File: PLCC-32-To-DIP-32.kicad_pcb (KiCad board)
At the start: 2 copper layers, 41.9 x 19 mm, 2 parts, among them U1 27C080, U2 27C080

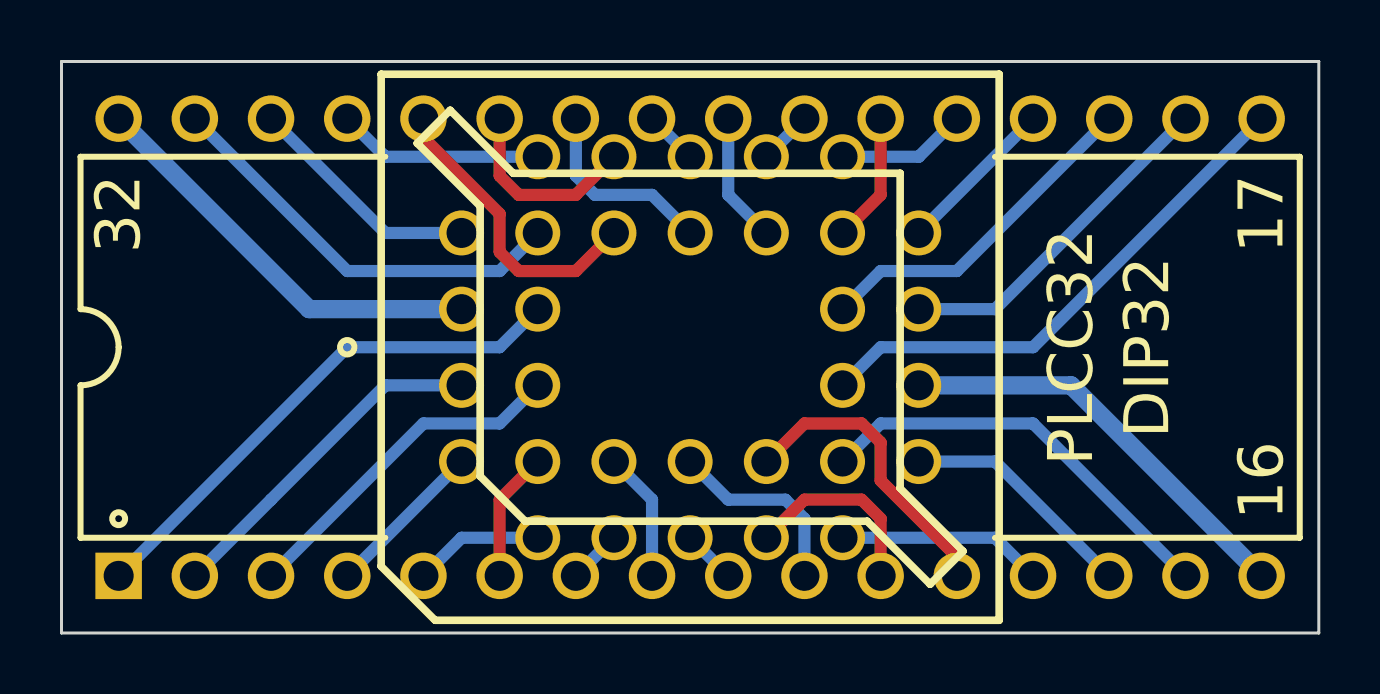
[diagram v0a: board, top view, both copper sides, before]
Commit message: Fixed gerber settings. Gerber output
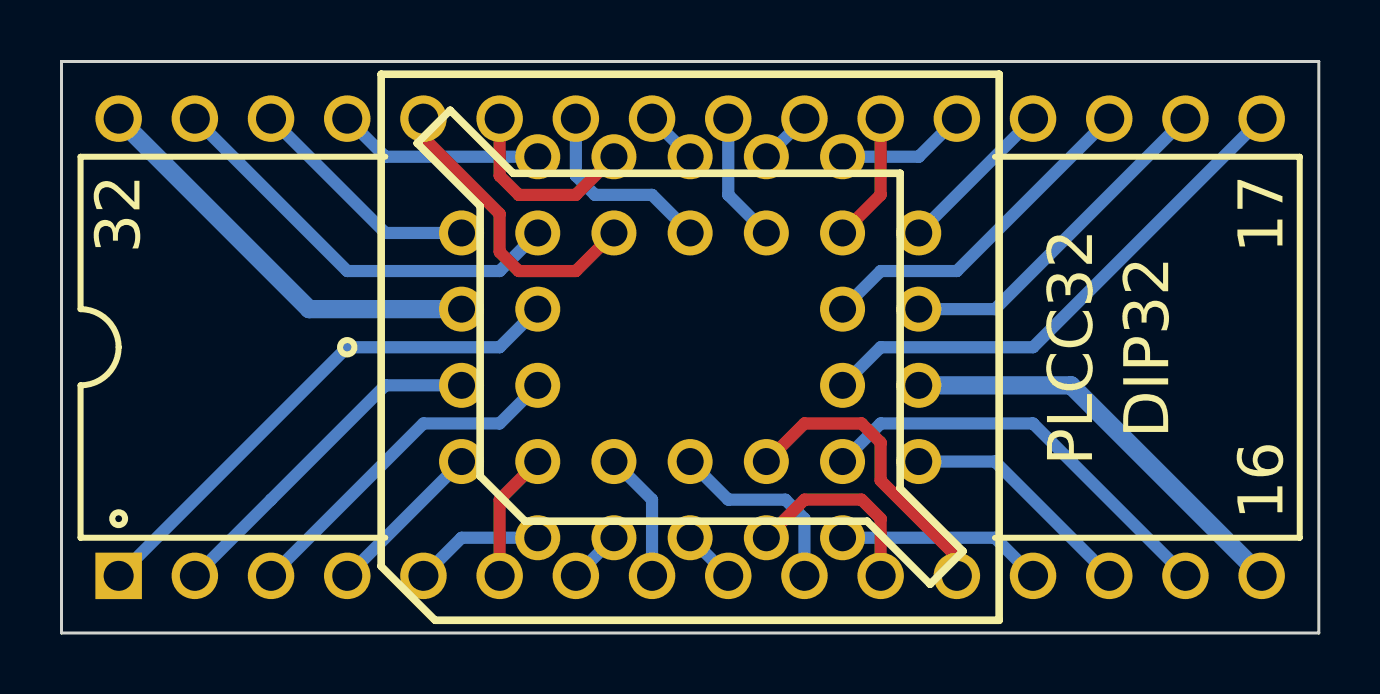
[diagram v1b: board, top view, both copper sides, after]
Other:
- rule pad_to_mask_clearance: 0 -> 0.1016
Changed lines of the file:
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@@
     (links 32)
     (no_connects 0)
-    (area 126.555499 95.834999 181.355 122.080001)
+    (area 127.584999 95.834999 181.355 122.080001)
     (thickness 1.6)
     (drawings 12)
@@
     (mod_text_width 0.1524)
     (pad_size 1.5 1.5)
-    (pad_drill 1)
-    (pad_to_mask_clearance 0)
-    (aux_axis_origin 0 0)
+    (pad_drill 0.9)
+    (pad_to_mask_clearance 0.1016)
+    (aux_axis_origin 127.635 114.935)
     (visible_elements FFFFFF7F)
     (pcbplotparams
-      (layerselection 3178497)
+      (layerselection 283148289)
       (usegerberextensions true)
       (excludeedgelayer true)
@@
       (viasonmask false)
       (mode 1)
-      (useauxorigin false)
+      (useauxorigin true)
       (hpglpennumber 1)
       (hpglpenspeed 20)
@@
       (plotinvisibletext false)
       (padsonsilk false)
-      (subtractmaskfromsilk false)
+      (subtractmaskfromsilk true)
       (outputformat 1)
       (mirror false)
-      (drillshape 1)
+      (drillshape 0)
       (scaleselection 1)
-      (outputdirectory ""))
+      (outputdirectory gerbers/))
   )
   (net 0 "")
@@
     (fp_line (start -7.8994 8.001) (end -6.79958 9.10082) (layer F.SilkS) (width 0.254))
     (fp_line (start -6.79958 9.09574) (end -4.70154 6.9977) (layer F.SilkS) (width 0.254))
-    (pad 2 thru_hole circle (at 1.27 7.62 270) (size 1.5 1.5) (drill 1)
+    (pad 2 thru_hole circle (at 1.27 7.62 270) (size 1.5 1.5) (drill 0.9)
       (layers *.Cu *.Mask F.SilkS)
       (net 9 /A16)
     )
-    (pad 1 thru_hole circle (at -1.27 5.08 270) (size 1.5 1.5) (drill 1)
+    (pad 1 thru_hole circle (at -1.27 5.08 270) (size 1.5 1.5) (drill 0.9)
       (layers *.Cu *.Mask F.SilkS)
       (net 12 /A19)
     )
-    (pad 3 thru_hole circle (at 1.27 5.08 270) (size 1.5 1.5) (drill 1)
+    (pad 3 thru_hole circle (at 1.27 5.08 270) (size 1.5 1.5) (drill 0.9)
       (layers *.Cu *.Mask F.SilkS)
       (net 8 /A15)
     )
-    (pad 4 thru_hole circle (at 3.81 7.62 270) (size 1.5 1.5) (drill 1)
+    (pad 4 thru_hole circle (at 3.81 7.62 270) (size 1.5 1.5) (drill 0.9)
       (layers *.Cu *.Mask F.SilkS)
       (net 5 /A12)
     )
-    (pad 5 thru_hole circle (at 6.35 5.08 270) (size 1.5 1.5) (drill 1)
+    (pad 5 thru_hole circle (at 6.35 5.08 270) (size 1.5 1.5) (drill 0.9)
       (layers *.Cu *.Mask F.SilkS)
       (net 18 /A7)
     )
-    (pad 6 thru_hole circle (at 3.81 5.08 270) (size 1.5 1.5) (drill 1)
+    (pad 6 thru_hole circle (at 3.81 5.08 270) (size 1.5 1.5) (drill 0.9)
       (layers *.Cu *.Mask F.SilkS)
       (net 17 /A6)
     )
-    (pad 7 thru_hole circle (at 6.35 2.54 270) (size 1.5 1.5) (drill 1)
+    (pad 7 thru_hole circle (at 6.35 2.54 270) (size 1.5 1.5) (drill 0.9)
       (layers *.Cu *.Mask F.SilkS)
       (net 16 /A5)
     )
-    (pad 8 thru_hole circle (at 3.81 2.54 270) (size 1.5 1.5) (drill 1)
+    (pad 8 thru_hole circle (at 3.81 2.54 270) (size 1.5 1.5) (drill 0.9)
       (layers *.Cu *.Mask F.SilkS)
       (net 15 /A4)
     )
-    (pad 9 thru_hole circle (at 6.35 0 270) (size 1.5 1.5) (drill 1)
+    (pad 9 thru_hole circle (at 6.35 0 270) (size 1.5 1.5) (drill 0.9)
       (layers *.Cu *.Mask F.SilkS)
       (net 14 /A3)
     )
-    (pad 10 thru_hole circle (at 3.81 0 270) (size 1.5 1.5) (drill 1)
+    (pad 10 thru_hole circle (at 3.81 0 270) (size 1.5 1.5) (drill 0.9)
       (layers *.Cu *.Mask F.SilkS)
       (net 13 /A2)
     )
-    (pad 11 thru_hole circle (at 6.35 -2.54 270) (size 1.5 1.5) (drill 1)
+    (pad 11 thru_hole circle (at 6.35 -2.54 270) (size 1.5 1.5) (drill 0.9)
       (layers *.Cu *.Mask F.SilkS)
       (net 2 /A1)
     )
-    (pad 12 thru_hole circle (at 3.81 -2.54 270) (size 1.5 1.5) (drill 1)
+    (pad 12 thru_hole circle (at 3.81 -2.54 270) (size 1.5 1.5) (drill 0.9)
       (layers *.Cu *.Mask F.SilkS)
       (net 1 /A0)
     )
-    (pad 13 thru_hole circle (at 6.35 -5.08 270) (size 1.5 1.5) (drill 1)
+    (pad 13 thru_hole circle (at 6.35 -5.08 270) (size 1.5 1.5) (drill 0.9)
       (layers *.Cu *.Mask F.SilkS)
       (net 22 /D0)
     )
-    (pad 14 thru_hole circle (at 3.81 -7.62 270) (size 1.5 1.5) (drill 1)
+    (pad 14 thru_hole circle (at 3.81 -7.62 270) (size 1.5 1.5) (drill 0.9)
       (layers *.Cu *.Mask F.SilkS)
       (net 23 /D1)
     )
-    (pad 15 thru_hole circle (at 3.81 -5.08 270) (size 1.5 1.5) (drill 1)
+    (pad 15 thru_hole circle (at 3.81 -5.08 270) (size 1.5 1.5) (drill 0.9)
       (layers *.Cu *.Mask F.SilkS)
       (net 24 /D2)
     )
-    (pad 16 thru_hole circle (at 1.27 -7.62 270) (size 1.5 1.5) (drill 1)
+    (pad 16 thru_hole circle (at 1.27 -7.62 270) (size 1.5 1.5) (drill 0.9)
       (layers *.Cu *.Mask F.SilkS)
       (net 31 GND)
     )
-    (pad 17 thru_hole circle (at 1.27 -5.08 270) (size 1.5 1.5) (drill 1)
+    (pad 17 thru_hole circle (at 1.27 -5.08 270) (size 1.5 1.5) (drill 0.9)
       (layers *.Cu *.Mask F.SilkS)
       (net 25 /D3)
     )
-    (pad 18 thru_hole circle (at -1.27 -7.62 270) (size 1.5 1.5) (drill 1)
+    (pad 18 thru_hole circle (at -1.27 -7.62 270) (size 1.5 1.5) (drill 0.9)
       (layers *.Cu *.Mask F.SilkS)
       (net 26 /D4)
     )
-    (pad 19 thru_hole circle (at -1.27 -5.08 270) (size 1.5 1.5) (drill 1)
+    (pad 19 thru_hole circle (at -1.27 -5.08 270) (size 1.5 1.5) (drill 0.9)
       (layers *.Cu *.Mask F.SilkS)
       (net 27 /D5)
     )
-    (pad 20 thru_hole circle (at -3.81 -7.62 270) (size 1.5 1.5) (drill 1)
+    (pad 20 thru_hole circle (at -3.81 -7.62 270) (size 1.5 1.5) (drill 0.9)
       (layers *.Cu *.Mask F.SilkS)
       (net 28 /D6)
     )
-    (pad 21 thru_hole circle (at -6.35 -5.08 270) (size 1.5 1.5) (drill 1)
+    (pad 21 thru_hole circle (at -6.35 -5.08 270) (size 1.5 1.5) (drill 0.9)
       (layers *.Cu *.Mask F.SilkS)
       (net 29 /D7)
     )
-    (pad 22 thru_hole circle (at -3.81 -5.08 270) (size 1.5 1.5) (drill 1)
+    (pad 22 thru_hole circle (at -3.81 -5.08 270) (size 1.5 1.5) (drill 0.9)
       (layers *.Cu *.Mask F.SilkS)
       (net 21 /CE)
     )
-    (pad 23 thru_hole circle (at -6.35 -2.54 270) (size 1.5 1.5) (drill 1)
+    (pad 23 thru_hole circle (at -6.35 -2.54 270) (size 1.5 1.5) (drill 0.9)
       (layers *.Cu *.Mask F.SilkS)
       (net 3 /A10)
     )
-    (pad 24 thru_hole circle (at -3.81 -2.54 270) (size 1.5 1.5) (drill 1)
+    (pad 24 thru_hole circle (at -3.81 -2.54 270) (size 1.5 1.5) (drill 0.9)
       (layers *.Cu *.Mask F.SilkS)
       (net 30 /OE)
     )
-    (pad 25 thru_hole circle (at -6.35 0 270) (size 1.5 1.5) (drill 1)
+    (pad 25 thru_hole circle (at -6.35 0 270) (size 1.5 1.5) (drill 0.9)
       (layers *.Cu *.Mask F.SilkS)
       (net 4 /A11)
     )
-    (pad 26 thru_hole circle (at -3.81 0 270) (size 1.5 1.5) (drill 1)
+    (pad 26 thru_hole circle (at -3.81 0 270) (size 1.5 1.5) (drill 0.9)
       (layers *.Cu *.Mask F.SilkS)
       (net 20 /A9)
     )
-    (pad 27 thru_hole circle (at -6.35 2.54 270) (size 1.5 1.5) (drill 1)
+    (pad 27 thru_hole circle (at -6.35 2.54 270) (size 1.5 1.5) (drill 0.9)
       (layers *.Cu *.Mask F.SilkS)
       (net 19 /A8)
     )
-    (pad 32 thru_hole circle (at -1.27 7.62 270) (size 1.5 1.5) (drill 1)
+    (pad 32 thru_hole circle (at -1.27 7.62 270) (size 1.5 1.5) (drill 0.9)
       (layers *.Cu *.Mask F.SilkS)
       (net 32 VCC)
     )
-    (pad 28 thru_hole circle (at -3.81 2.54 270) (size 1.5 1.5) (drill 1)
+    (pad 28 thru_hole circle (at -3.81 2.54 270) (size 1.5 1.5) (drill 0.9)
       (layers *.Cu *.Mask F.SilkS)
       (net 6 /A13)
     )
-    (pad 29 thru_hole circle (at -6.35 5.08 270) (size 1.5 1.5) (drill 1)
+    (pad 29 thru_hole circle (at -6.35 5.08 270) (size 1.5 1.5) (drill 0.9)
       (layers *.Cu *.Mask F.SilkS)
       (net 7 /A14)
     )
-    (pad 30 thru_hole circle (at -3.81 7.62 270) (size 1.5 1.5) (drill 1)
+    (pad 30 thru_hole circle (at -3.81 7.62 270) (size 1.5 1.5) (drill 0.9)
       (layers *.Cu *.Mask F.SilkS)
       (net 10 /A17)
     )
-    (pad 31 thru_hole circle (at -3.81 5.08 270) (size 1.5 1.5) (drill 1)
+    (pad 31 thru_hole circle (at -3.81 5.08 270) (size 1.5 1.5) (drill 0.9)
       (layers *.Cu *.Mask F.SilkS)
       (net 11 /A18)
